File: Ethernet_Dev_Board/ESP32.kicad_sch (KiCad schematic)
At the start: 10 parts, among them J1 TAG-CONNECT_NL_10-POS_LEGS, U6 ESP32-WROOM-32E, U7 74LVC1G11W6

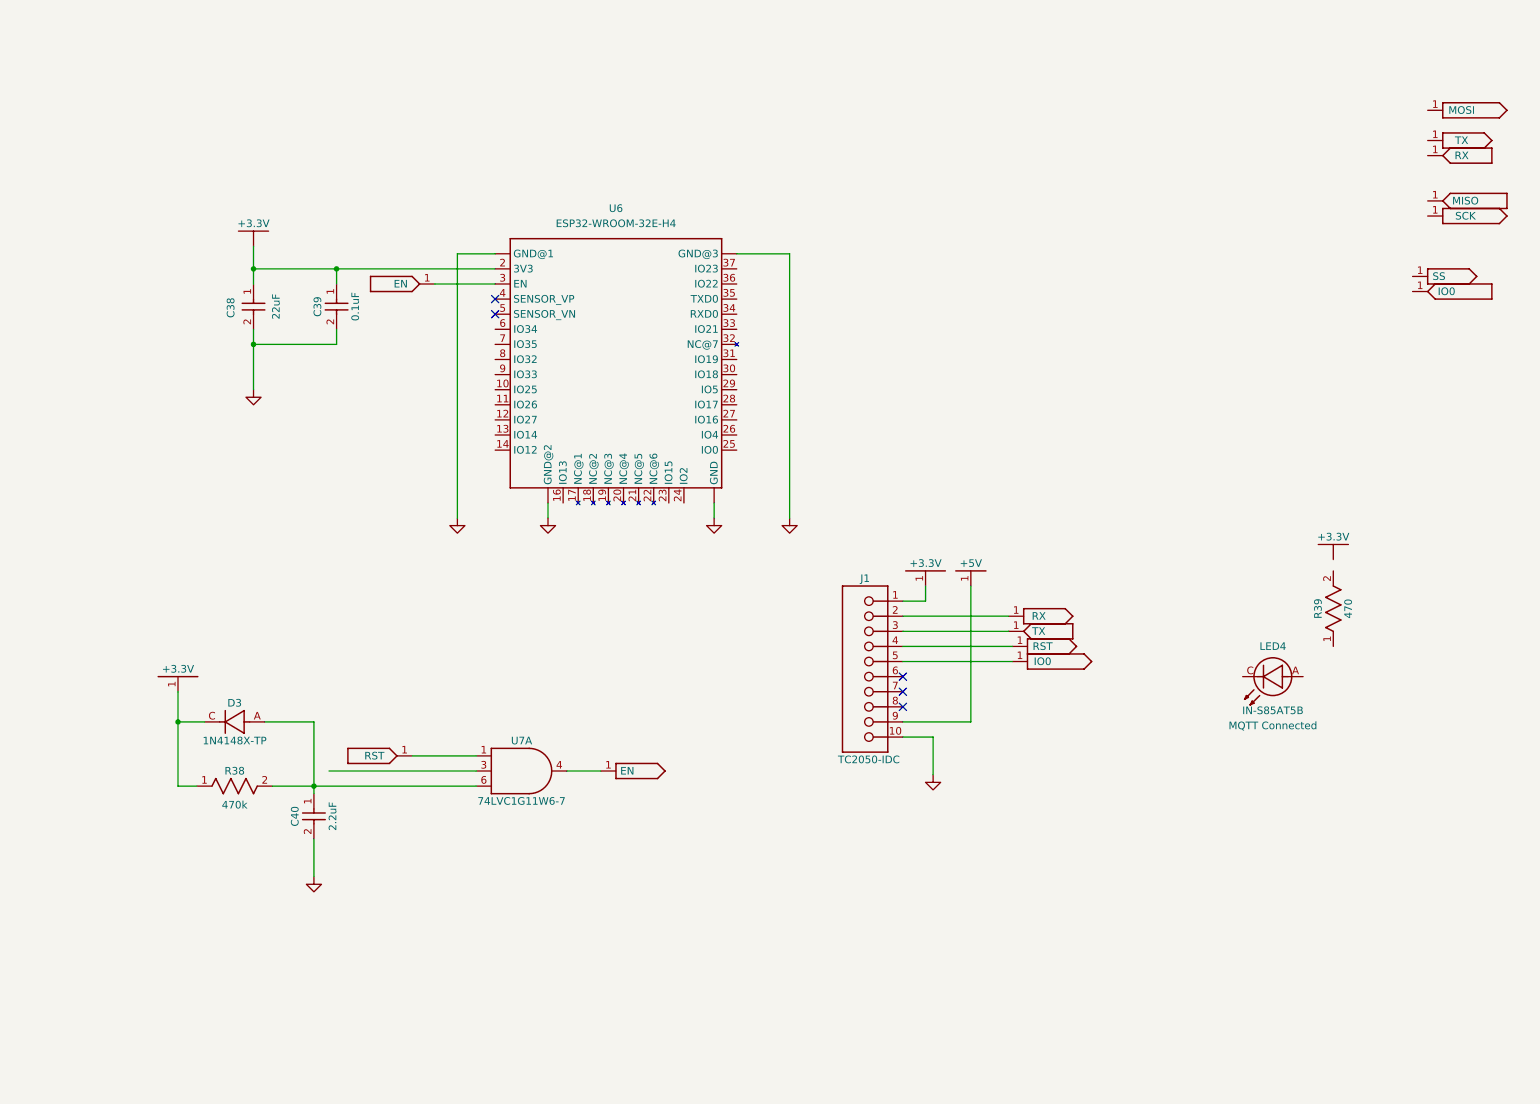
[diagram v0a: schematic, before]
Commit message: Added in ESP circuit
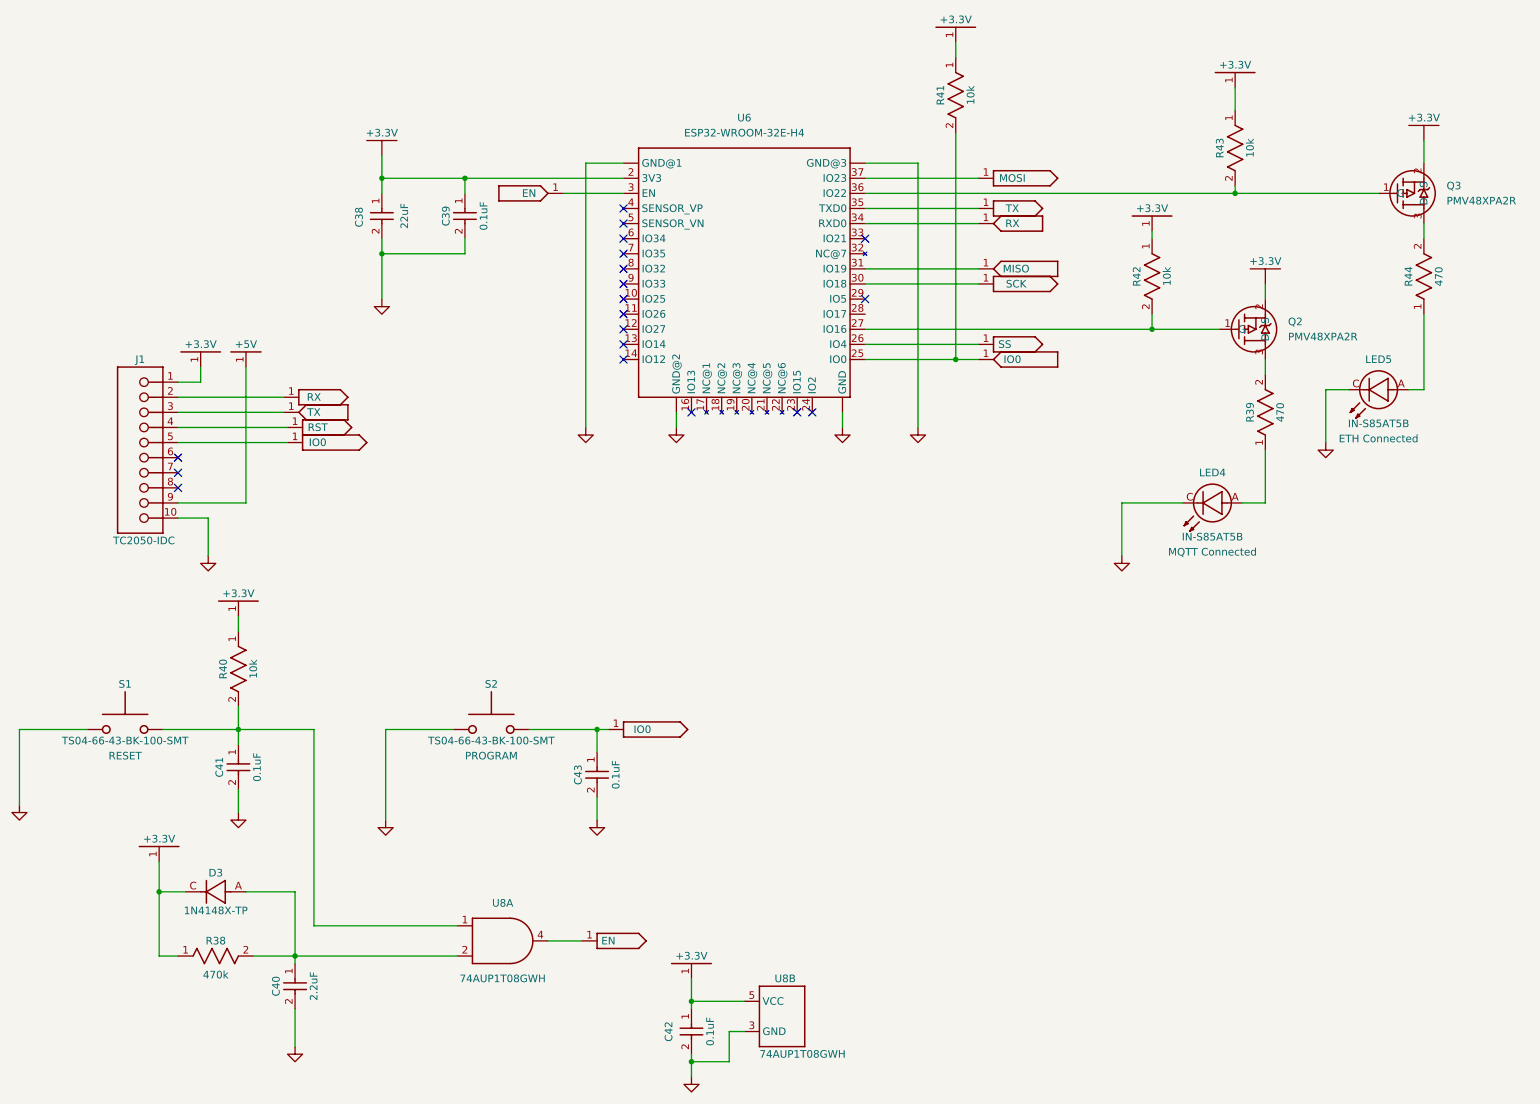
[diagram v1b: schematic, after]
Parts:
- removed U7: 74LVC1G11W6, RG_TO_SOT_SMD:SOT23-6, symbol LED_Controller_Hardware-eagle-import:74LVC1G11W6
- added C41, C42, C43: 0.1uF, RG_Capacitors_SMD:0603, symbol LED_Controller_Hardware-eagle-import:CAP-0603
- added LED5: ETH Connected, RG_Diode:0805-D, symbol RG_Diode:LED
- added Q2, Q3: PMV48XPA2R, RG_TO_SOT_SMD:SOT23-3P95, symbol RG_FETs:PMV48XPA2R
- added R40, R41, R42, R43: 10k, RG_Resistors_SMD:0603, symbol LED_Controller_Hardware-eagle-import:RES-0603
- added R44: 470, RG_Resistors_SMD:0603, symbol LED_Controller_Hardware-eagle-import:RES-0603
- added S1: RESET, RG_Switches:SW_TS04-66-65-BK-260-SMT, symbol LED_Controller_Hardware-eagle-import:RESET
- added S2: PROGRAM, RG_Switches:SW_TS04-66-65-BK-260-SMT, symbol LED_Controller_Hardware-eagle-import:PROGRAM
- added U8: 74AUP1T08GWH, RG_TO_SOT_SMD:SOT23-5P65, symbol RG_Logic:74AUP1T08GWH
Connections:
- net +3.3V: now also C42.1, Q2.2 (S), Q3.2 (S), R40.1, R41.1, R42.1, R43.1, U8.5 (VCC)
- net EN: now also U8.4 (Y)
- net GNDS: now also LED4.C, C41.2, C42.2, C43.2, LED5.C, S1.2 (1), S1.4 (1), S2.2 (1), S2.4 (1), U8.3 (GND)
- net IO0: now also U6.25 (IO0), C43.1, R41.2, S2.1 (2), S2.3 (2)
- net MISO: now also U6.31 (IO19)
- net MOSI: now also U6.37 (IO23)
- net RX: now also U6.34 (RXD0)
- net SCK: now also U6.30 (IO18)
- net SS: now also U6.26 (IO4)
- net TX: now also U6.35 (TXD0)
- net at U6.27 (IO16): now also Q2.1 (G), R42.2
- net at U6.36 (IO22): now also Q3.1 (G), R43.2
- net at C40.1, D3.A, R38.2: now also U8.2 (C)
- net at R39.1: now also LED4.A
- net at R39.2: now also Q2.3 (D)
- new net: C41.1, R40.2, S1.1 (2), S1.3 (2), U8.1 (A)
- new net: LED5.A, R44.1
- new net: Q3.3 (D), R44.2
- no-connect marks 5 -> 19
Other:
- moved on the sheet: C38, C39, C40, D3, J1, LED4, R38, R39, U6

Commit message: Added additional oscillator circuit. Re-annotated schematic
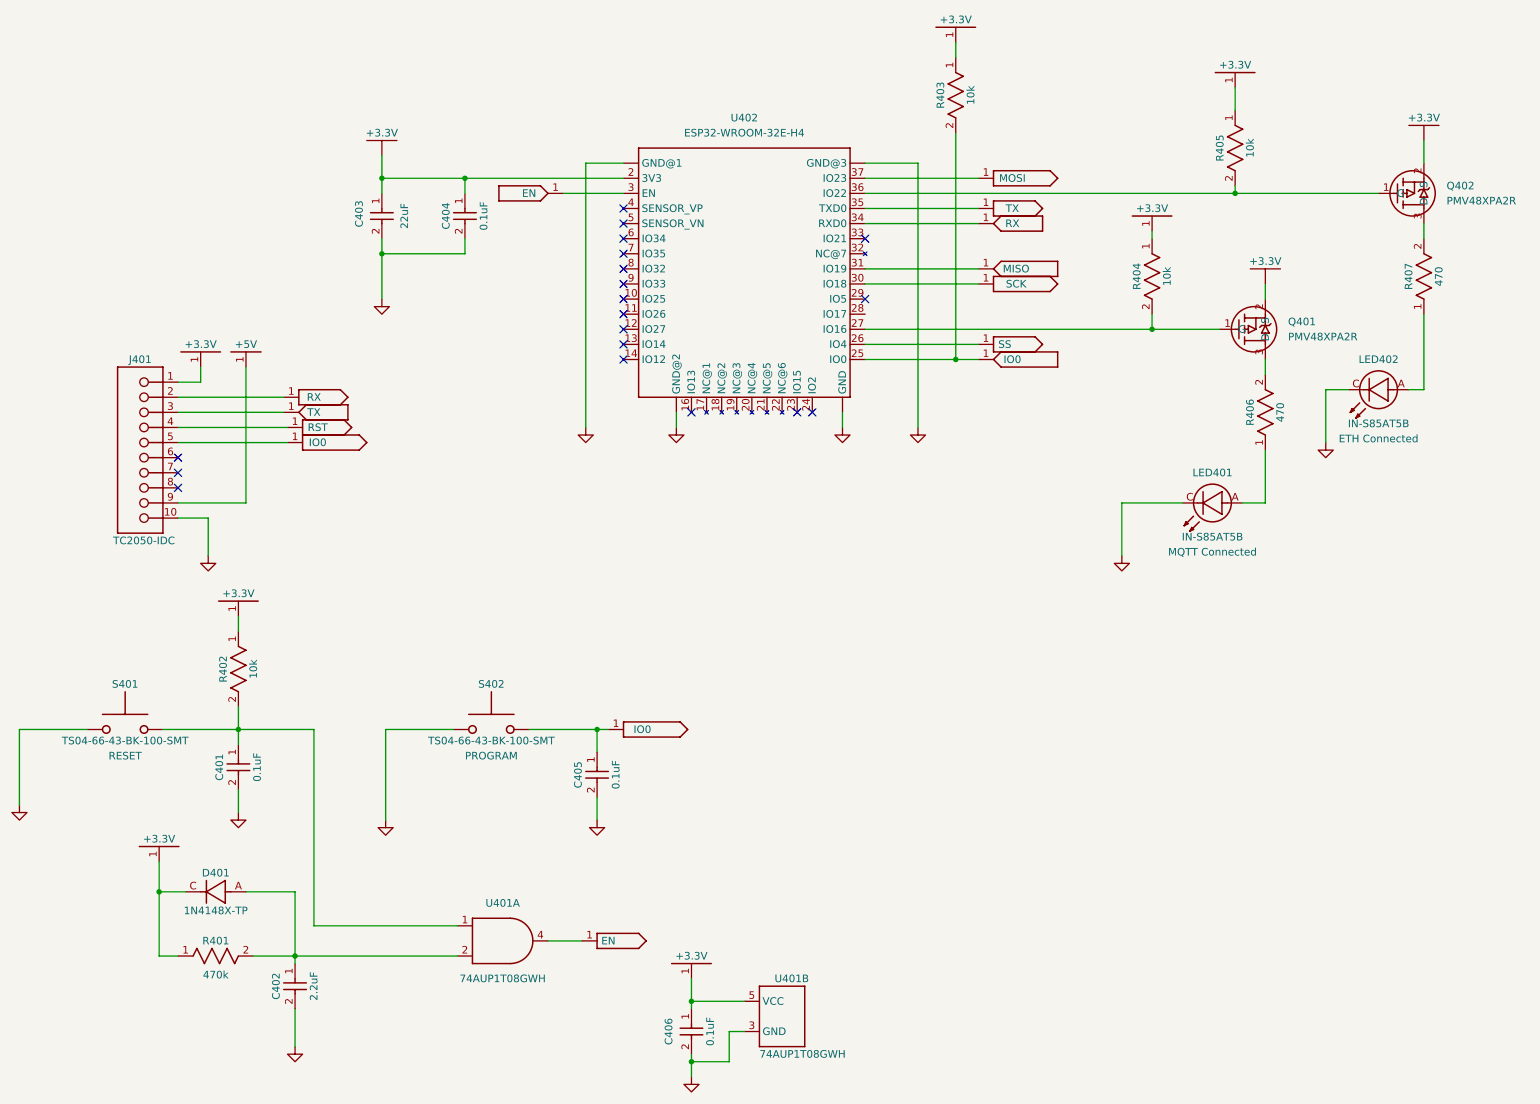
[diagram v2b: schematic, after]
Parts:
- renumbered C41 to C401, C40 to C402, C38 to C403, C39 to C404, C43 to C405, C42 to C406, D3 to D401, J1 to J401, LED4 to LED401, LED5 to LED402, Q2 to Q401, Q3 to Q402, R38 to R401, R40 to R402, R41 to R403, R42 to R404, R43 to R405, R39 to R406, R44 to R407, S1 to S401, S2 to S402, U8 to U401, U6 to U402
